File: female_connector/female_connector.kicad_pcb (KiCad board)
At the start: 2 copper layers, 40.6 x 22.2 mm, 6 parts, among them J1 Conn_02x07_Row_Letter_Last, J2 Conn_02x12_Row_Letter_Last

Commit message: pcb finalized, very exciting
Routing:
- net /CAN3_H: track 10.6 -> 19.2 mm
- net /CAN2_L: track 16.5 -> 22.1 mm
- net /SBU2: track 14.9 -> 20.3 mm
- net /CAN2_H: track 18.7 -> 24.0 mm
- net /SBU1: track 11.4 -> 6.30 mm
- net /CAN0_L: track 11.0 -> 6.95 mm
- net /CAN1_L: track 11.0 -> 6.95 mm
- net /CAN1_H: track 12.5 -> 8.80 mm
- net /CAN0_H: track 12.5 -> 8.80 mm
- net /CAN3_L: track 13.8 -> 16.6 mm
- net GND: track 33.9 -> 36.7 mm

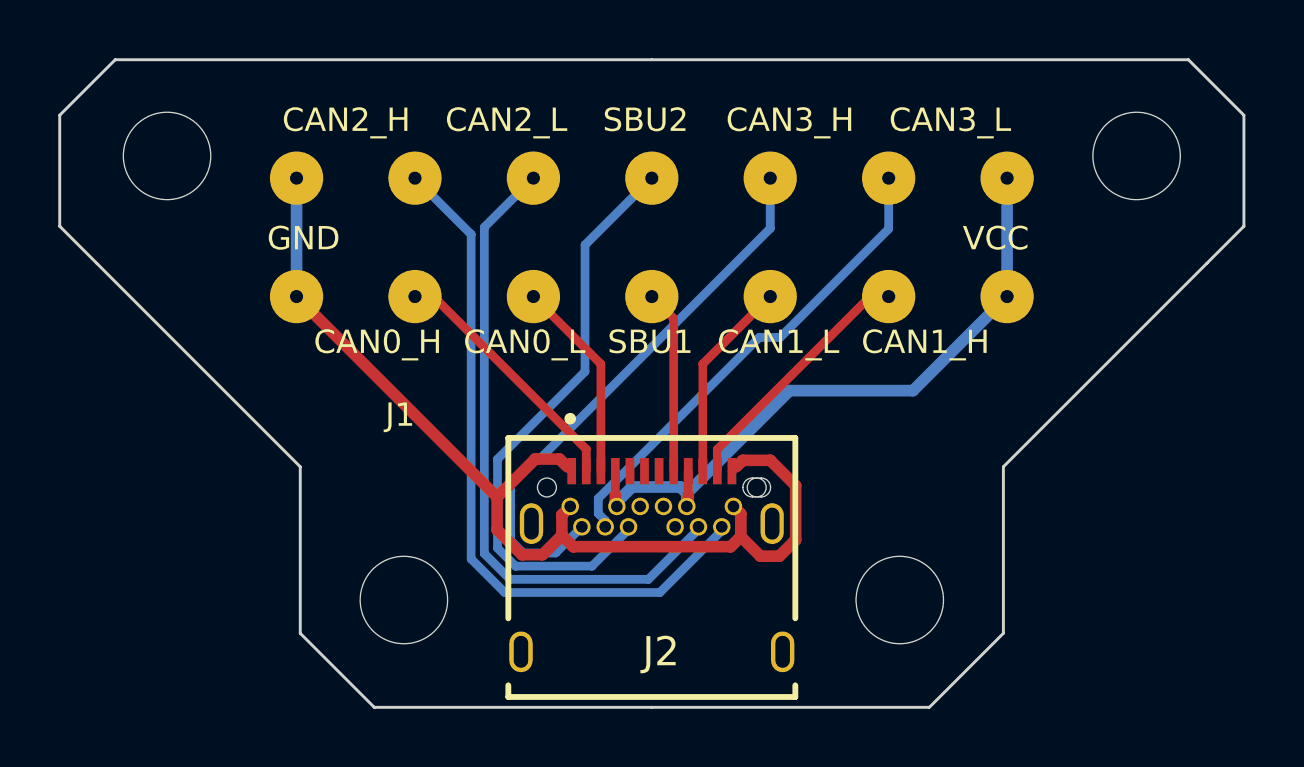
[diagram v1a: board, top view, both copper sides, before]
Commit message: generate gerber files for production
Orders have been submitted to manufacturer for evaluation.
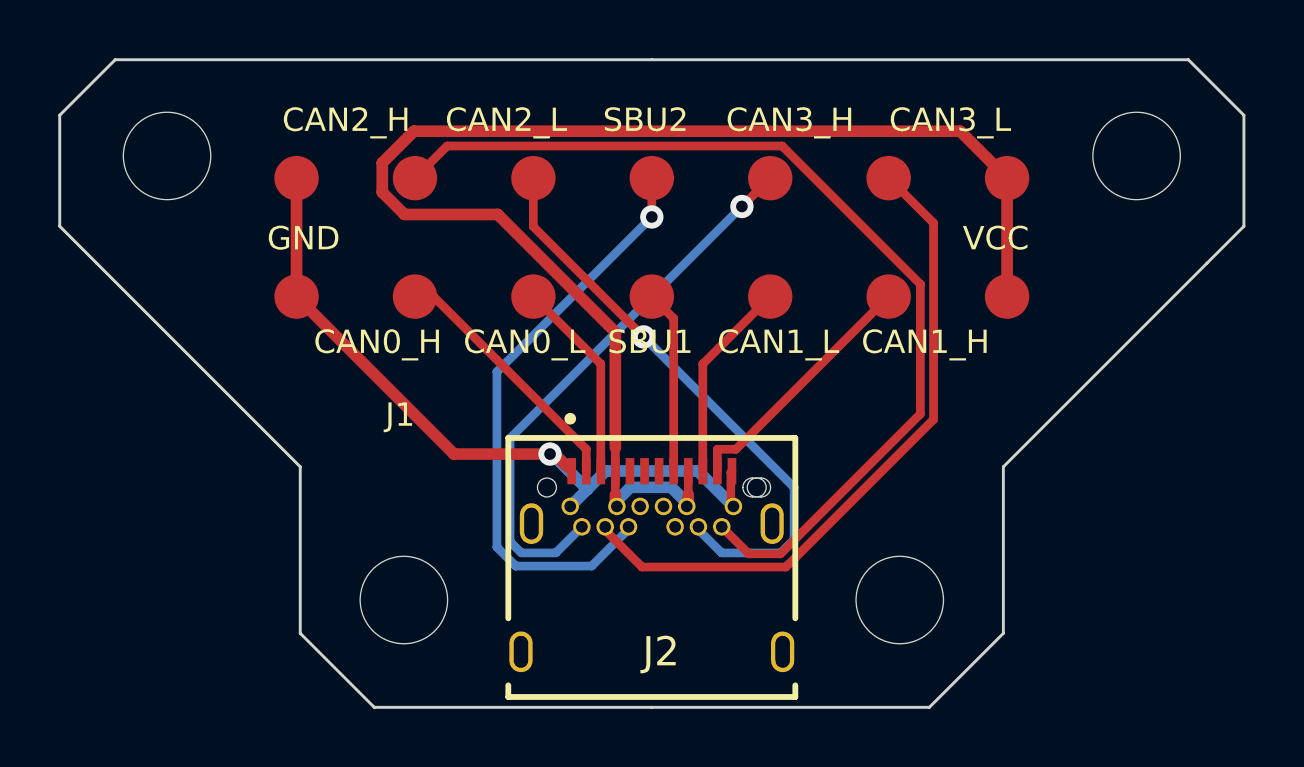
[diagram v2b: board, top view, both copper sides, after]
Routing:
- net +12V: track 23.6 -> 48.0 mm
- net GND: track 36.7 -> 25.6 mm, vias 0 -> 1
- net /CAN2_H: track 24.0 -> 33.4 mm
- net /CAN3_L: track 16.6 -> 22.9 mm
- net /CAN2_L: track 22.1 -> 20.0 mm, vias 0 -> 1
- net /CAN3_H: vias 0 -> 1
- net /SBU2: vias 0 -> 1

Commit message: increased female smd pad size for slop
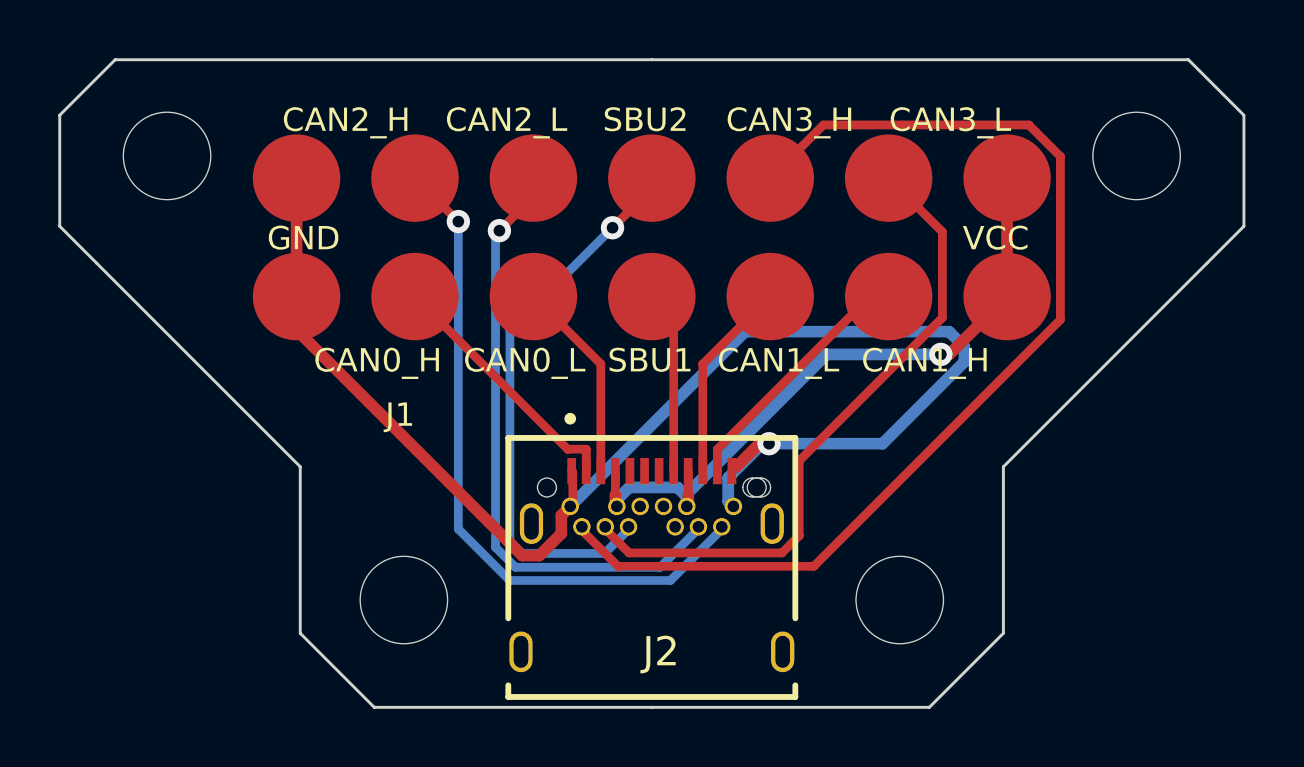
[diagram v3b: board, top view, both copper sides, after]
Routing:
- net +12V: track 48.0 -> 23.7 mm, vias 0 -> 1
- net GND: track 25.6 -> 49.3 mm
- net /CAN3_H: track 19.2 -> 37.3 mm, vias 1 -> 0
- net /CAN2_H: track 33.4 -> 23.2 mm, vias 0 -> 1
- net /SBU2: track 20.3 -> 19.2 mm
- net /CAN2_L: track 20.0 -> 21.1 mm
- net /CAN3_L: track 22.9 -> 22.4 mm
